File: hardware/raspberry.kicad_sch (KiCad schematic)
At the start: 19 parts, among them J1 Conn_01x04, U1 W25Q128JVS, Y1 Crystal_GND24

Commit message: minor schematic changes
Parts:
- C10, C11, C12, C13, C14, C15, C2, C3, C4, C5, C6, C7, C8, C9: footprint Capacitor_SMD:C_0201_0603Metric -> Capacitor_SMD:C_0603_1608Metric
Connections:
- net +3V3: now also RASPBERRY_PI1.1 (IOVDD), RASPBERRY_PI1.10 (IOVDD), RASPBERRY_PI1.22 (IOVDD), RASPBERRY_PI1.33 (IOVDD), RASPBERRY_PI1.42 (IOVDD), RASPBERRY_PI1.43 (ADC_AVDD), RASPBERRY_PI1.44 (VREG_IN), RASPBERRY_PI1.48 (USB_VDD), RASPBERRY_PI1.49 (IOVDD)

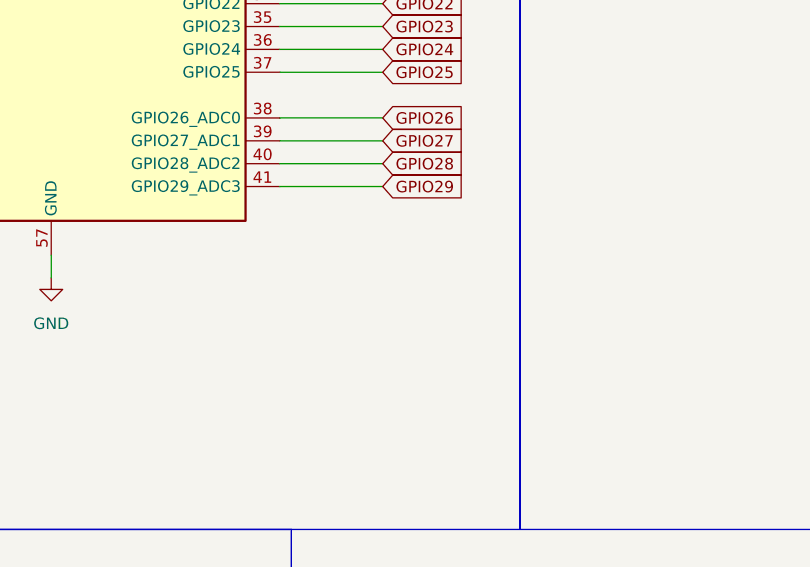
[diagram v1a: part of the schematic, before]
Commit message: output filter added
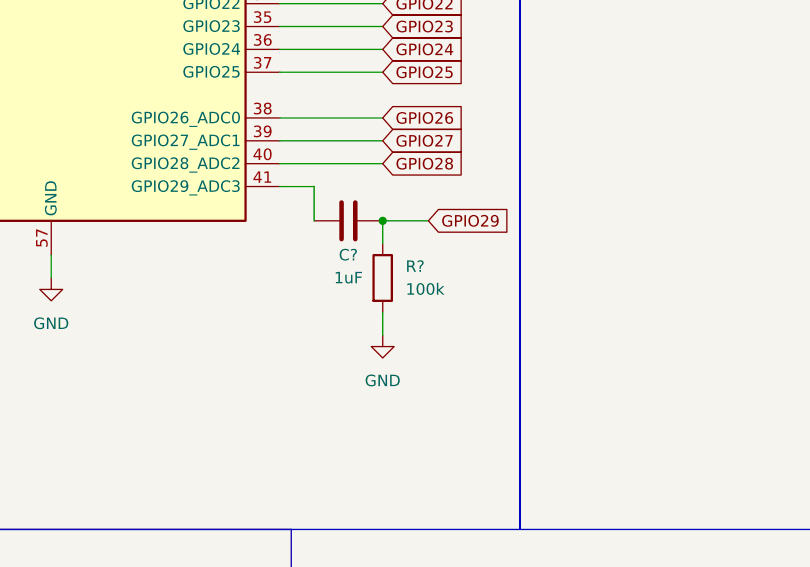
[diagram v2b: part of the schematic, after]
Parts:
- added C?: 1uF, Capacitor_SMD:C_0603_1608Metric, symbol Device:C
- added R?: 100k, Resistor_SMD:R_0603_1608Metric, symbol Device:R
- R2: footprint Resistor_SMD:R_0201_0603Metric -> Resistor_SMD:R_0603_1608Metric
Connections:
- net GND: now also R?.2
- net GPIO29: now also C?.2, R?.1; no longer RASPBERRY_PI1.41 (GPIO29_ADC3)
- new net: C?.1, RASPBERRY_PI1.41 (GPIO29_ADC3)

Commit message: raspberry pi pcb
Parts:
- J1: footprint Connector_PinHeader_2.54mm:PinHeader_1x04_P2.54mm_Vertical -> Connector_PinHeader_2.54mm:PinHeader_2x02_P2.54mm_Vertical
- gave numbers to parts that had none: 2
- renumbered C9 to C10, C10 to C11, C11 to C12, C12 to C13, C13 to C14, C14 to C15, C15 to C16, C6 to C7, C7 to C8, C8 to C9
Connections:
- net +3V3: now also C3.1
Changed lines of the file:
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@@
 	(wire
 		(pts
-			(xy 63.5 109.22) (xy 73.66 109.22)
+			(xy 63.5 109.22) (xy 76.2 109.22)
 		)
 		(stroke
@@
 	(wire
 		(pts
+			(xy 246.38 72.39) (xy 246.38 73.66)
+		)
+		(stroke
+			(width 0)
+			(type default)
+		)
+	)
+	(wire
+		(pts
 			(xy 46.99 49.53) (xy 53.34 49.53)
 		)
@@
 	(hierarchical_label "XOUT"
 		(shape input)
-		(at 73.66 109.22 0)
+		(at 76.2 109.22 0)
 		(effects
 			(font
@@
 		(dnp no)
 		(fields_autoplaced yes)
-		(property "Reference" "#PWR024"
+		(property "Reference" "#PWR025"
 			(at 115.57 195.58 0)
 			(effects
@@
 			(project "flute"
 				(path "/9ae53f79-8ce2-4a44-ba8e-dca375125c34/739c4558-e5ce-473d-85db-8208f7847074"
-					(reference "#PWR024")
+					(reference "#PWR025")
 					(unit 1)
 				)
@@
 		(on_board yes)
 		(dnp no)
-		(property "Reference" "C8"
+		(property "Reference" "C9"
 			(at 70.104 180.34 0)
 			(effects
@@
 			(project "flute"
 				(path "/9ae53f79-8ce2-4a44-ba8e-dca375125c34/739c4558-e5ce-473d-85db-8208f7847074"
-					(reference "C8")
+					(reference "C9")
 					(unit 1)
 				)
@@
 		(dnp no)
 		(fields_autoplaced yes)
-		(property "Reference" "#PWR021"
+		(property "Reference" "#PWR022"
 			(at 76.2 195.58 0)
 			(effects
@@
 			(project "flute"
 				(path "/9ae53f79-8ce2-4a44-ba8e-dca375125c34/739c4558-e5ce-473d-85db-8208f7847074"
-					(reference "#PWR021")
+					(reference "#PWR022")
 					(unit 1)
 				)
@@
 		(on_board yes)
 		(dnp no)
-		(property "Reference" "C11"
+		(property "Reference" "C12"
 			(at 109.474 180.34 0)
 			(effects
@@
 			(project "flute"
 				(path "/9ae53f79-8ce2-4a44-ba8e-dca375125c34/739c4558-e5ce-473d-85db-8208f7847074"
-					(reference "C11")
+					(reference "C12")
 					(unit 1)
 				)
@@
 		(on_board yes)
 		(dnp no)
-		(property "Reference" "C15"
+		(property "Reference" "C16"
 			(at 155.194 180.34 0)
 			(effects
@@
 			(project "flute"
 				(path "/9ae53f79-8ce2-4a44-ba8e-dca375125c34/739c4558-e5ce-473d-85db-8208f7847074"
-					(reference "C15")
+					(reference "C16")
 					(unit 1)
 				)
@@
 		(on_board yes)
 		(dnp no)
-		(property "Reference" "#PWR015"
+		(property "Reference" "#PWR016"
 			(at 54.61 177.8 0)
 			(effects
@@
 			(project "flute"
 				(path "/9ae53f79-8ce2-4a44-ba8e-dca375125c34/739c4558-e5ce-473d-85db-8208f7847074"
-					(reference "#PWR015")
+					(reference "#PWR016")
 					(unit 1)
 				)
@@
 		(dnp no)
 		(fields_autoplaced yes)
-		(property "Reference" "#PWR026"
+		(property "Reference" "#PWR027"
 			(at 138.43 195.58 0)
 			(effects
@@
 			(project "flute"
 				(path "/9ae53f79-8ce2-4a44-ba8e-dca375125c34/739c4558-e5ce-473d-85db-8208f7847074"
-					(reference "#PWR026")
+					(reference "#PWR027")
 					(unit 1)
 				)
@@
 		(on_board yes)
 		(dnp no)
-		(property "Reference" "C14"
+		(property "Reference" "C15"
 			(at 143.764 180.34 0)
 			(effects
@@
 			(project "flute"
 				(path "/9ae53f79-8ce2-4a44-ba8e-dca375125c34/739c4558-e5ce-473d-85db-8208f7847074"
-					(reference "C14")
+					(reference "C15")
 					(unit 1)
 				)
@@
 		(dnp no)
 		(fields_autoplaced yes)
-		(property "Reference" "#PWR017"
+		(property "Reference" "#PWR018"
 			(at 86.36 173.99 0)
 			(effects
@@
 			(project "flute"
 				(path "/9ae53f79-8ce2-4a44-ba8e-dca375125c34/739c4558-e5ce-473d-85db-8208f7847074"
-					(reference "#PWR017")
+					(reference "#PWR018")
 					(unit 1)
 				)
@@
 		(on_board yes)
 		(dnp no)
-		(property "Reference" "C7"
+		(property "Reference" "C8"
 			(at 57.404 180.34 0)
 			(effects
@@
 			(project "flute"
 				(path "/9ae53f79-8ce2-4a44-ba8e-dca375125c34/739c4558-e5ce-473d-85db-8208f7847074"
-					(reference "C7")
+					(reference "C8")
 					(unit 1)
 				)
@@
 		(on_board yes)
 		(dnp no)
-		(property "Reference" "C10"
+		(property "Reference" "C11"
 			(at 98.044 180.34 0)
 			(effects
@@
 			(project "flute"
 				(path "/9ae53f79-8ce2-4a44-ba8e-dca375125c34/739c4558-e5ce-473d-85db-8208f7847074"
-					(reference "C10")
+					(reference "C11")
 					(unit 1)
 				)
@@
 		(on_board yes)
 		(dnp no)
-		(property "Reference" "C9"
+		(property "Reference" "C10"
 			(at 84.074 180.34 0)
 			(effects
@@
 			(project "flute"
 				(path "/9ae53f79-8ce2-4a44-ba8e-dca375125c34/739c4558-e5ce-473d-85db-8208f7847074"
-					(reference "C9")
+					(reference "C10")
 					(unit 1)
 				)
@@
 		(dnp no)
 		(fields_autoplaced yes)
-		(property "Reference" "#PWR018"
+		(property "Reference" "#PWR019"
 			(at 157.48 173.99 0)
 			(effects
@@
 			(project "flute"
 				(path "/9ae53f79-8ce2-4a44-ba8e-dca375125c34/739c4558-e5ce-473d-85db-8208f7847074"
-					(reference "#PWR018")
+					(reference "#PWR019")
 					(unit 1)
 				)
@@
 		(dnp no)
 		(fields_autoplaced yes)
-		(property "Reference" "#PWR028"
+		(property "Reference" "#PWR029"
 			(at 161.29 195.58 0)
 			(effects
@@
 			(project "flute"
 				(path "/9ae53f79-8ce2-4a44-ba8e-dca375125c34/739c4558-e5ce-473d-85db-8208f7847074"
-					(reference "#PWR028")
+					(reference "#PWR029")
 					(unit 1)
 				)
@@
 		(on_board yes)
 		(dnp no)
-		(property "Reference" "C12"
+		(property "Reference" "C13"
 			(at 120.904 180.34 0)
 			(effects
@@
 			(project "flute"
 				(path "/9ae53f79-8ce2-4a44-ba8e-dca375125c34/739c4558-e5ce-473d-85db-8208f7847074"
-					(reference "C12")
+					(reference "C13")
 					(unit 1)
 				)
@@
 			)
 		)
-		(property "Footprint" "Connector_PinHeader_2.54mm:PinHeader_1x04_P2.54mm_Vertical"
+		(property "Footprint" "Connector_PinHeader_2.54mm:PinHeader_2x02_P2.54mm_Vertical"
 			(at 58.42 52.07 0)
 			(effects
@@
 		(dnp no)
 		(fields_autoplaced yes)
-		(property "Reference" "#PWR016"
+		(property "Reference" "#PWR017"
 			(at 72.39 173.99 0)
 			(effects
@@
 			(project "flute"
 				(path "/9ae53f79-8ce2-4a44-ba8e-dca375125c34/739c4558-e5ce-473d-85db-8208f7847074"
-					(reference "#PWR016")
+					(reference "#PWR017")
 					(unit 1)
 				)
@@
 		(dnp no)
 		(fields_autoplaced yes)
-		(property "Reference" "#PWR020"
+		(property "Reference" "#PWR021"
 			(at 63.5 195.58 0)
 			(effects
@@
 			(project "flute"
 				(path "/9ae53f79-8ce2-4a44-ba8e-dca375125c34/739c4558-e5ce-473d-85db-8208f7847074"
-					(reference "#PWR020")
+					(reference "#PWR021")
 					(unit 1)
 				)
@@
 		(dnp no)
 		(fields_autoplaced yes)
-		(property "Reference" "R?"
+		(property "Reference" "R3"
 			(at 190.5 138.4299 0)
 			(effects
@@
 			(project ""
 				(path "/9ae53f79-8ce2-4a44-ba8e-dca375125c34/739c4558-e5ce-473d-85db-8208f7847074"
-					(reference "R?")
+					(reference "R3")
 					(unit 1)
 				)
@@
 		(on_board yes)
 		(dnp no)
-		(property "Reference" "C6"
+		(property "Reference" "C7"
 			(at 40.894 180.34 0)
 			(effects
@@
 			(project "flute"
 				(path "/9ae53f79-8ce2-4a44-ba8e-dca375125c34/739c4558-e5ce-473d-85db-8208f7847074"
-					(reference "C6")
+					(reference "C7")
 					(unit 1)
 				)
@@
 		(dnp no)
 		(fields_autoplaced yes)
-		(property "Reference" "#PWR029"
+		(property "Reference" "#PWR015"
 			(at 187.96 152.4 0)
 			(effects
@@
 			(project ""
 				(path "/9ae53f79-8ce2-4a44-ba8e-dca375125c34/739c4558-e5ce-473d-85db-8208f7847074"
-					(reference "#PWR029")
+					(reference "#PWR015")
 					(unit 1)
 				)
@@
 		(dnp no)
 		(fields_autoplaced yes)
-		(property "Reference" "#PWR022"
+		(property "Reference" "#PWR023"
 			(at 90.17 195.58 0)
 			(effects
@@
 			(project "flute"
 				(path "/9ae53f79-8ce2-4a44-ba8e-dca375125c34/739c4558-e5ce-473d-85db-8208f7847074"
-					(reference "#PWR022")
+					(reference "#PWR023")
 					(unit 1)
 				)
@@
 		(on_board yes)
 		(dnp no)
-		(property "Reference" "C13"
+		(property "Reference" "C14"
 			(at 132.334 180.34 0)
 			(effects
@@
 			(project "flute"
 				(path "/9ae53f79-8ce2-4a44-ba8e-dca375125c34/739c4558-e5ce-473d-85db-8208f7847074"
-					(reference "C13")
+					(reference "C14")
 					(unit 1)
 				)
@@
 		(dnp no)
 		(fields_autoplaced yes)
-		(property "Reference" "#PWR019"
+		(property "Reference" "#PWR020"
 			(at 46.99 195.58 0)
 			(effects
@@
 			(project "flute"
 				(path "/9ae53f79-8ce2-4a44-ba8e-dca375125c34/739c4558-e5ce-473d-85db-8208f7847074"
-					(reference "#PWR019")
+					(reference "#PWR020")
 					(unit 1)
 				)
@@
 		(dnp no)
 		(fields_autoplaced yes)
-		(property "Reference" "#PWR025"
+		(property "Reference" "#PWR026"
 			(at 127 195.58 0)
 			(effects
@@
 			(project "flute"
 				(path "/9ae53f79-8ce2-4a44-ba8e-dca375125c34/739c4558-e5ce-473d-85db-8208f7847074"
-					(reference "#PWR025")
+					(reference "#PWR026")
 					(unit 1)
 				)
@@
 		(dnp no)
 		(fields_autoplaced yes)
-		(property "Reference" "#PWR023"
+		(property "Reference" "#PWR024"
 			(at 104.14 195.58 0)
 			(effects
@@
 			(project "flute"
 				(path "/9ae53f79-8ce2-4a44-ba8e-dca375125c34/739c4558-e5ce-473d-85db-8208f7847074"
-					(reference "#PWR023")
+					(reference "#PWR024")
 					(unit 1)
 				)
@@
 		(on_board yes)
 		(dnp no)
-		(property "Reference" "C?"
+		(property "Reference" "C6"
 			(at 184.15 137.16 90)
 			(effects
@@
 			(project ""
 				(path "/9ae53f79-8ce2-4a44-ba8e-dca375125c34/739c4558-e5ce-473d-85db-8208f7847074"
-					(reference "C?")
+					(reference "C6")
 					(unit 1)
 				)
@@
 		(dnp no)
 		(fields_autoplaced yes)
-		(property "Reference" "#PWR027"
+		(property "Reference" "#PWR028"
 			(at 149.86 195.58 0)
 			(effects
@@
 			(project "flute"
 				(path "/9ae53f79-8ce2-4a44-ba8e-dca375125c34/739c4558-e5ce-473d-85db-8208f7847074"
-					(reference "#PWR027")
+					(reference "#PWR028")
 					(unit 1)
 				)

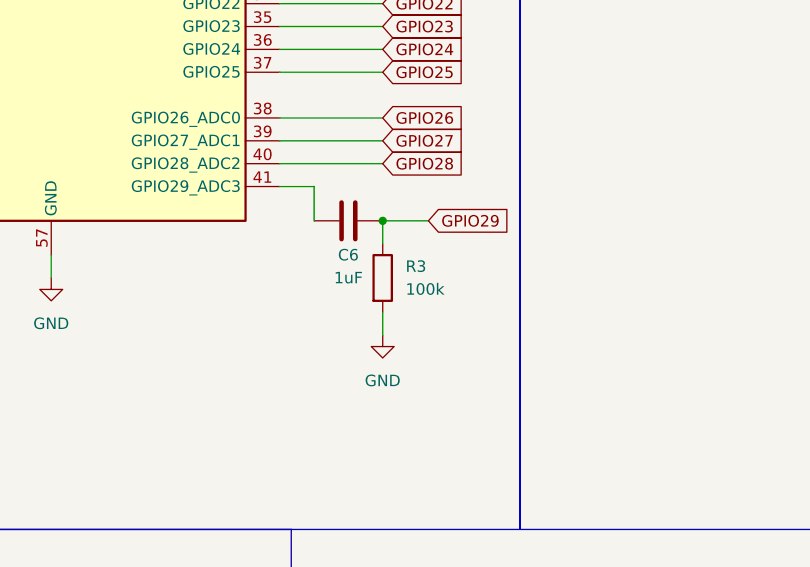
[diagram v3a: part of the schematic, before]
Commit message: added jack and battery
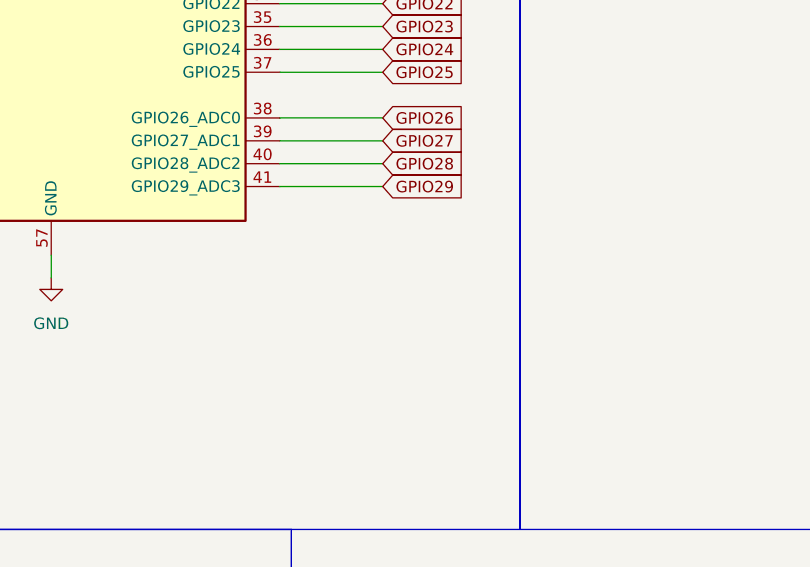
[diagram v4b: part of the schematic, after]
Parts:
- removed C6: 1uF, Capacitor_SMD:C_0603_1608Metric, symbol Device:C
- removed R3: 100k, Resistor_SMD:R_0603_1608Metric, symbol Device:R
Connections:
- net GPIO29: now also RASPBERRY_PI1.41 (GPIO29_ADC3)

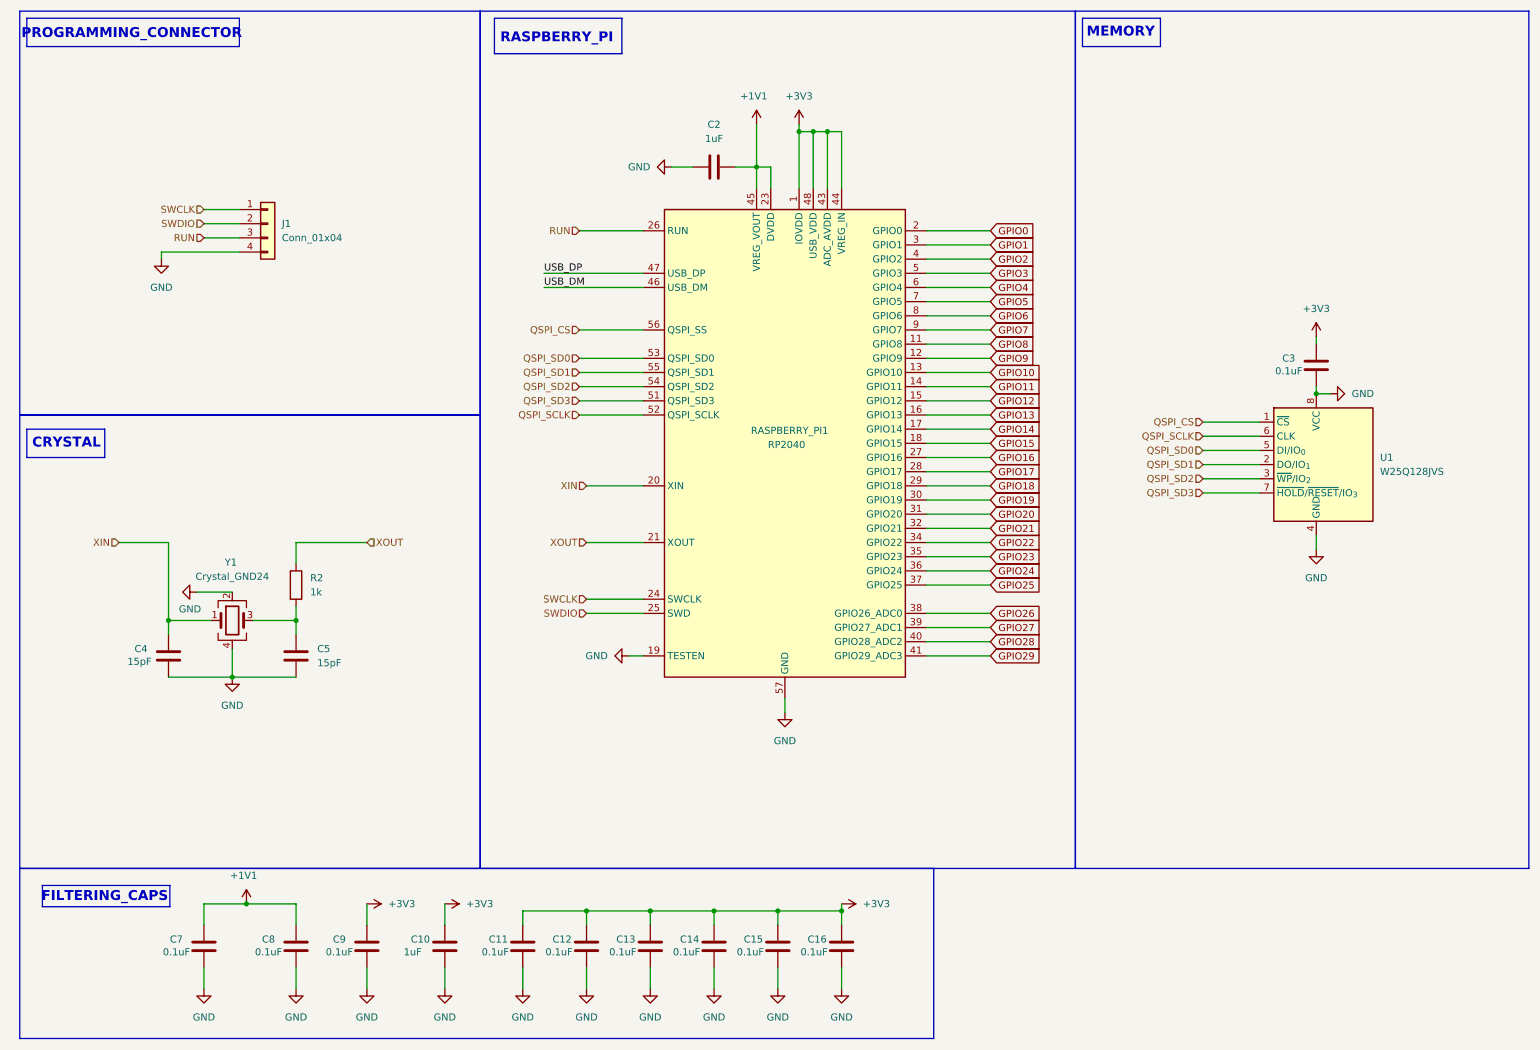
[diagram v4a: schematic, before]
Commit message: type of connections changed
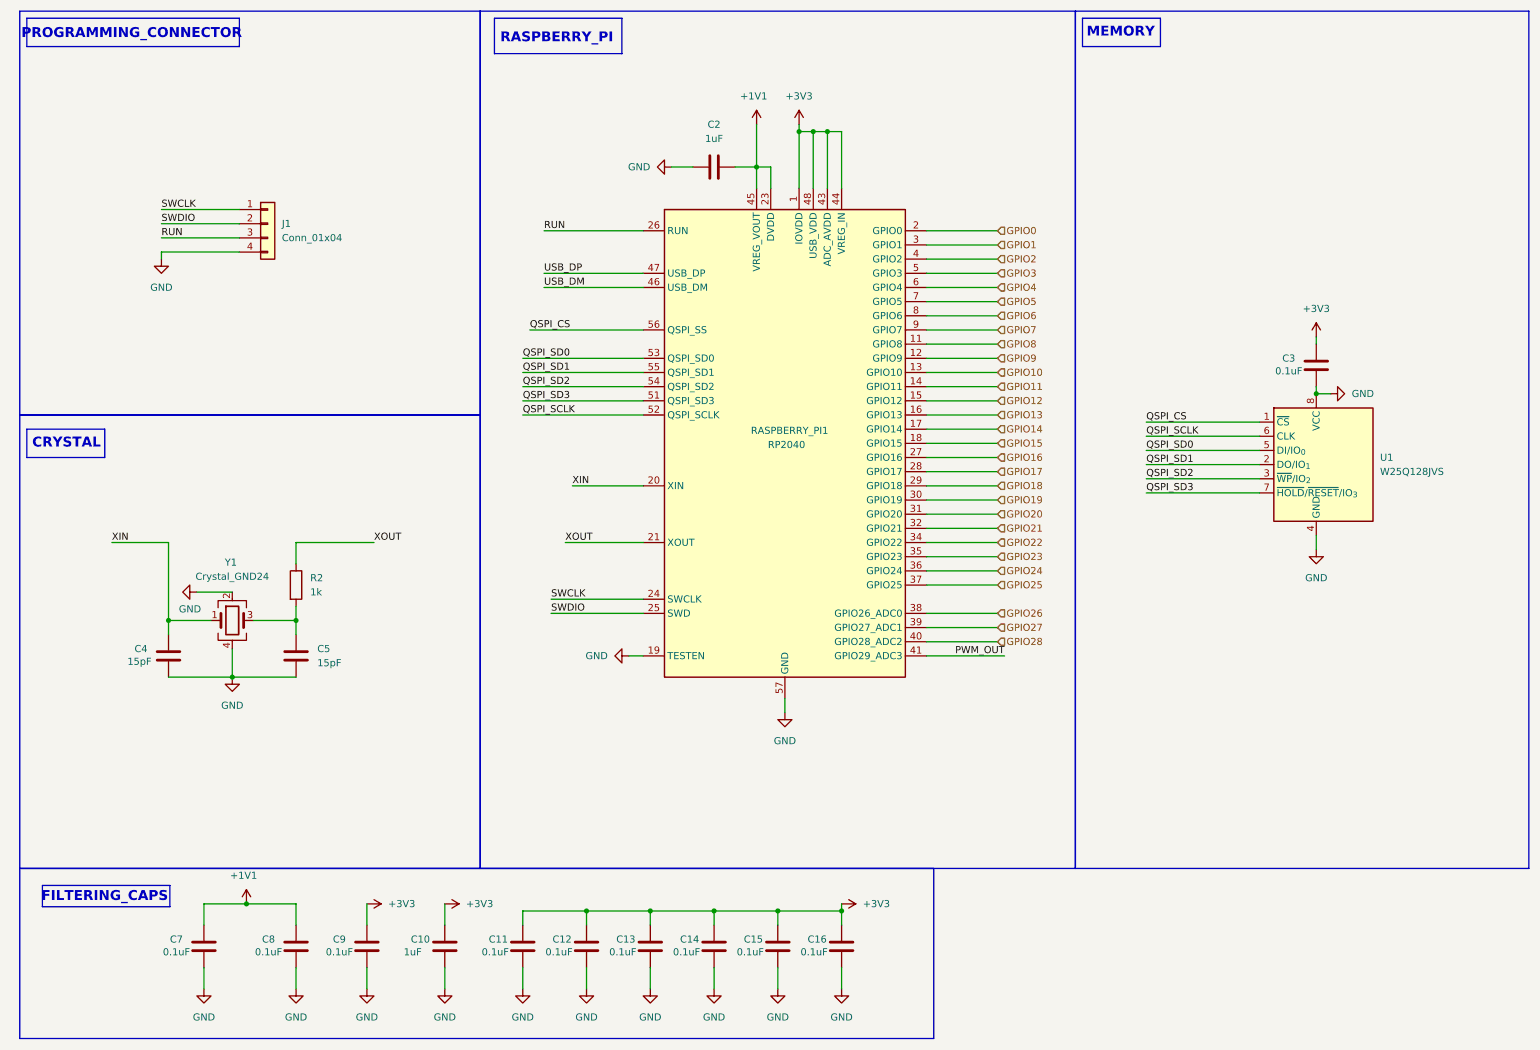
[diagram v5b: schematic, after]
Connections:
- net GPIO29 renamed PWM_OUT

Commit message: complete pcb ver1
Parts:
- renumbered C12 to C10, C13 to C11, C2 to C12, C14 to C13, C15 to C14, C16 to C15, C3 to C16, C4 to C3, C7 to C4, C8 to C6, C9 to C7, C10 to C8, C11 to C9, J1 to J3, R2 to R3, RASPBERRY_PI1 to U1, U1 to U2
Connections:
- net SWCLK: now also J3.2 (Pin_2); no longer J3.1 (Pin_1)
- net SWDIO: now also J3.1 (Pin_1); no longer J3.2 (Pin_2)
- net PWM_OUT renamed GPIO29
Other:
- company: (none) -> KN HARDWIRE AGH
- title: (none) -> MINIMALISED RASBERRY PI PICO
